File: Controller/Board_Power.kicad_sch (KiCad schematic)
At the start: 80 parts, among them J10 Screw_Terminal_01x08, J59 USB4140-GF-0070-C_REVA3, J60 Conn_01x03_Pin, U13 LMR51625, U15 LM76005RNPR, U8 LM706A0RRXR, U9 LM706A0RRXR

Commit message: Fixed some minor issues, started some scheamtic clean up
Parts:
- TP6, TP7, TP8: now not fitted
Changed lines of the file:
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@@
 		(exclude_from_sim no)
 		(in_bom yes)
-		(on_board yes)
-		(dnp no)
+		(on_board no)
+		(dnp yes)
 		(fields_autoplaced yes)
 		(property "Reference" "TP7"
@@
 		(exclude_from_sim no)
 		(in_bom yes)
-		(on_board yes)
-		(dnp no)
+		(on_board no)
+		(dnp yes)
 		(fields_autoplaced yes)
 		(property "Reference" "TP8"
@@
 		(exclude_from_sim no)
 		(in_bom yes)
-		(on_board yes)
-		(dnp no)
+		(on_board no)
+		(dnp yes)
 		(fields_autoplaced yes)
 		(property "Reference" "TP6"

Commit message: Reconfigured 12v & 5v buck converteres
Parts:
- removed C151, C152, C153: 1uF, Capacitor_SMD:C_1206_3216Metric, symbol Device:C
- removed C154, C155: 100nF, Capacitor_SMD:C_0603_1608Metric, symbol Device:C
- removed C156: 18pF, Capacitor_SMD:C_0402_1005Metric, symbol Device:C
- removed C157, C158, C159: 47uF, Capacitor_SMD:C_0805_2012Metric, symbol Device:C
- removed L4: 8.2uH, Inductor_SMD:L_Bourns-SRN4018, symbol Device:L_Small
- removed R8: 24K, Resistor_SMD:R_0603_1608Metric, symbol Device:R
- removed R9: 7K68, Resistor_SMD:R_0603_1608Metric, symbol Device:R
- removed U13: LMR51625, Package_TO_SOT_SMD:SOT-23-6, symbol IC:LMR51625
- C178: value 200pF -> 82pF
- C179: value 220pF -> 2.2nF
- C180: value 12nF -> 22pF
- C181: value 10nF -> 5.6nF
- L5: value 3.3uH -> 6.8uH; LCSC C970536 -> C970538
- R12: value R004 -> R005; LCSC C46634448 -> (none)
- R13: value R004 -> R005
- R16: value 52K3 -> 26K7
- R24: value 3K57 -> 6K65
- R25: value 2K87 -> 7K5
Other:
- note removed: "24V-48V to 3.3V <2A"
- note removed: "TODO: check inductor footprint"
- moved on the sheet: F1, F2, F3, J10, TP6, TP7, TP8

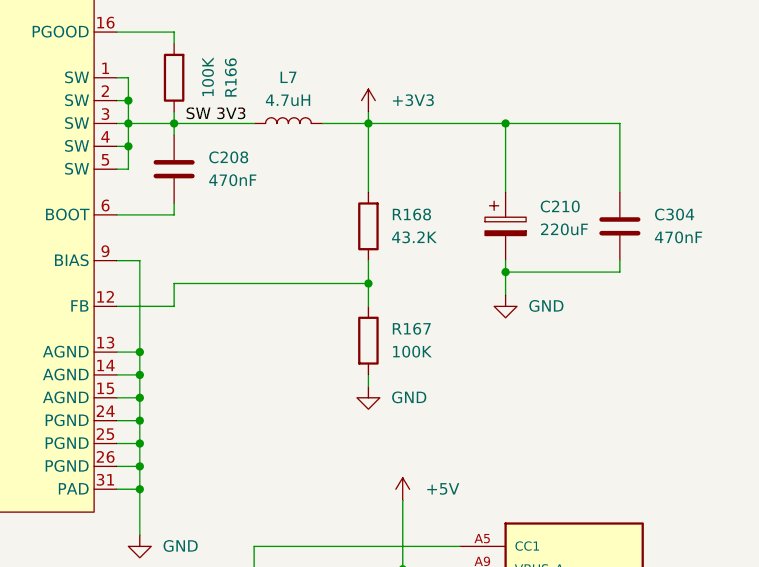
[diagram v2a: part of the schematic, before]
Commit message: DDR_CLK termination
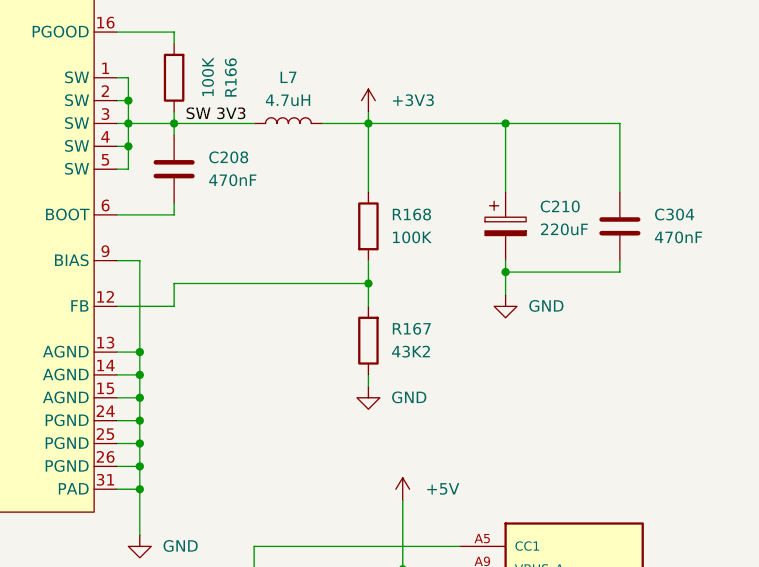
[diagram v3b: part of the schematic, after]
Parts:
- R167: value 100K -> 43K2
- R168: value 43.2K -> 100K
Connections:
- net +3V3: now also R168.1; no longer R168.2
- net GND: now also R167.1; no longer R167.2
- new net: R167.2, R168.2, U15.12 (FB)
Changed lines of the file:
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@@
 	(symbol
 		(lib_id "Device:R")
+		(at 365.76 83.82 0)
+		(unit 1)
+		(body_style 1)
+		(exclude_from_sim no)
+		(in_bom yes)
+		(on_board yes)
+		(in_pos_files yes)
+		(dnp no)
+		(fields_autoplaced yes)
+		(property "Reference" "R168"
+			(at 368.3 82.5499 0)
+			(show_name no)
+			(do_not_autoplace no)
+			(effects
+				(font
+					(size 1.27 1.27)
+				)
+				(justify left)
+			)
+		)
+		(property "Value" "100K"
+			(at 368.3 85.0899 0)
+			(show_name no)
+			(do_not_autoplace no)
+			(effects
+				(font
+					(size 1.27 1.27)
+				)
+				(justify left)
+			)
+		)
+		(property "Footprint" "Resistor_SMD:R_0603_1608Metric"
+			(at 363.982 83.82 90)
+			(hide yes)
+			(show_name no)
+			(do_not_autoplace no)
+			(effects
+				(font
+					(size 1.27 1.27)
+				)
+			)
+		)
+		(property "Datasheet" ""
+			(at 365.76 83.82 0)
+			(hide yes)
+			(show_name no)
+			(do_not_autoplace no)
+			(effects
+				(font
+					(size 1.27 1.27)
+				)
+			)
+		)
+		(property "Description" "Resistor"
+			(at 365.76 83.82 0)
+			(hide yes)
+			(show_name no)
+			(do_not_autoplace no)
+			(effects
+				(font
+					(size 1.27 1.27)
+				)
+			)
+		)
+		(pin "2"
+		)
+		(pin "1"
+		)
+		(instances
+			(project "Controller"
+				(path "/2c9e7a41-63e4-4339-89dd-991e772f7a19/be892fd5-6ed8-4ba2-a1e8-7916f9f879fe"
+					(reference "R168")
+					(unit 1)
+				)
+			)
+		)
+	)
+	(symbol
+		(lib_id "Device:R")
 		(at 330.2 213.36 0)
 		(unit 1)
@@
 	)
 	(symbol
+		(lib_id "Device:R")
+		(at 365.76 96.52 180)
+		(unit 1)
+		(body_style 1)
+		(exclude_from_sim no)
+		(in_bom yes)
+		(on_board yes)
+		(in_pos_files yes)
+		(dnp no)
+		(fields_autoplaced yes)
+		(property "Reference" "R167"
+			(at 368.3 95.2499 0)
+			(show_name no)
+			(do_not_autoplace no)
+			(effects
+				(font
+					(size 1.27 1.27)
+				)
+				(justify right)
+			)
+		)
+		(property "Value" "43K2"
+			(at 368.3 97.7899 0)
+			(show_name no)
+			(do_not_autoplace no)
+			(effects
+				(font
+					(size 1.27 1.27)
+				)
+				(justify right)
+			)
+		)
+		(property "Footprint" "Resistor_SMD:R_0603_1608Metric"
+			(at 367.538 96.52 90)
+			(hide yes)
+			(show_name no)
+			(do_not_autoplace no)
+			(effects
+				(font
+					(size 1.27 1.27)
+				)
+			)
+		)
+		(property "Datasheet" ""
+			(at 365.76 96.52 0)
+			(hide yes)
+			(show_name no)
+			(do_not_autoplace no)
+			(effects
+				(font
+					(size 1.27 1.27)
+				)
+			)
+		)
+		(property "Description" "Resistor"
+			(at 365.76 96.52 0)
+			(hide yes)
+			(show_name no)
+			(do_not_autoplace no)
+			(effects
+				(font
+					(size 1.27 1.27)
+				)
+			)
+		)
+		(pin "2"
+		)
+		(pin "1"
+		)
+		(instances
+			(project "Controller"
+				(path "/2c9e7a41-63e4-4339-89dd-991e772f7a19/be892fd5-6ed8-4ba2-a1e8-7916f9f879fe"
+					(reference "R167")
+					(unit 1)
+				)
+			)
+		)
+	)
+	(symbol
 		(lib_id "power:GND")
 		(at 373.38 153.67 0)
@@
 	)
 	(symbol
-		(lib_id "Device:R")
-		(at 365.76 96.52 0)
-		(unit 1)
-		(body_style 1)
-		(exclude_from_sim no)
-		(in_bom yes)
-		(on_board yes)
-		(in_pos_files yes)
-		(dnp no)
-		(fields_autoplaced yes)
-		(property "Reference" "R167"
-			(at 368.3 95.2499 0)
-			(show_name no)
-			(do_not_autoplace no)
-			(effects
-				(font
-					(size 1.27 1.27)
-				)
-				(justify left)
-			)
-		)
-		(property "Value" "100K"
-			(at 368.3 97.7899 0)
-			(show_name no)
-			(do_not_autoplace no)
-			(effects
-				(font
-					(size 1.27 1.27)
-				)
-				(justify left)
-			)
-		)
-		(property "Footprint" "Resistor_SMD:R_0603_1608Metric"
-			(at 363.982 96.52 90)
-			(hide yes)
-			(show_name no)
-			(do_not_autoplace no)
-			(effects
-				(font
-					(size 1.27 1.27)
-				)
-			)
-		)
-		(property "Datasheet" ""
-			(at 365.76 96.52 0)
-			(hide yes)
-			(show_name no)
-			(do_not_autoplace no)
-			(effects
-				(font
-					(size 1.27 1.27)
-				)
-			)
-		)
-		(property "Description" "Resistor"
-			(at 365.76 96.52 0)
-			(hide yes)
-			(show_name no)
-			(do_not_autoplace no)
-			(effects
-				(font
-					(size 1.27 1.27)
-				)
-			)
-		)
-		(pin "2"
-		)
-		(pin "1"
-		)
-		(instances
-			(project "Controller"
-				(path "/2c9e7a41-63e4-4339-89dd-991e772f7a19/be892fd5-6ed8-4ba2-a1e8-7916f9f879fe"
-					(reference "R167")
-					(unit 1)
-				)
-			)
-		)
-	)
-	(symbol
 		(lib_id "Connector:Conn_01x03_Pin")
 		(at 254 100.33 0)
@@
 					(unit 1)
 				)
-			)
-		)
-	)
-	(symbol
-		(lib_id "Device:R")
-		(at 365.76 83.82 180)
-		(unit 1)
-		(body_style 1)
-		(exclude_from_sim no)
-		(in_bom yes)
-		(on_board yes)
-		(in_pos_files yes)
-		(dnp no)
-		(fields_autoplaced yes)
-		(property "Reference" "R168"
-			(at 368.3 82.5499 0)
-			(show_name no)
-			(do_not_autoplace no)
-			(effects
-				(font
-					(size 1.27 1.27)
-				)
-				(justify right)
-			)
-		)
-		(property "Value" "43.2K"
-			(at 368.3 85.0899 0)
-			(show_name no)
-			(do_not_autoplace no)
-			(effects
-				(font
-					(size 1.27 1.27)
-				)
-				(justify right)
-			)
-		)
-		(property "Footprint" "Resistor_SMD:R_0603_1608Metric"
-			(at 367.538 83.82 90)
-			(hide yes)
-			(show_name no)
-			(do_not_autoplace no)
-			(effects
-				(font
-					(size 1.27 1.27)
-				)
-			)
-		)
-		(property "Datasheet" ""
-			(at 365.76 83.82 0)
-			(hide yes)
-			(show_name no)
-			(do_not_autoplace no)
-			(effects
-				(font
-					(size 1.27 1.27)
-				)
-			)
-		)
-		(property "Description" "Resistor"
-			(at 365.76 83.82 0)
-			(hide yes)
-			(show_name no)
-			(do_not_autoplace no)
-			(effects
-				(font
-					(size 1.27 1.27)
-				)
-			)
-		)
-		(pin "2"
-		)
-		(pin "1"
-		)
-		(instances
-			(project "Controller"
-				(path "/2c9e7a41-63e4-4339-89dd-991e772f7a19/be892fd5-6ed8-4ba2-a1e8-7916f9f879fe"
-					(reference "R168")
-					(unit 1)
-				)

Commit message: REV 1B
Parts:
- added D49, D50, D51: SM6T68A, Diode_SMD:D_SMB, symbol Diode:SM6T68A
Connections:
- net GND: now also D49.2 (A2), D50.2 (A2), D51.2 (A2)
- net VIN Board Fused: now also D49.1 (A1)
- net VIN Heat Fused: now also D51.1 (A1)
- net VIN Motor Fused: now also D50.1 (A1)
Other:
- moved on the sheet: F1, F2, F3, J10, TP6, TP7, TP8
